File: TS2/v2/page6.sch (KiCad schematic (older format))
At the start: 16 parts, among them SW2 SINGLE STEP/RUN, SW3 STEP, U10 74LS32, U19 74LS20, U20 74LS74, U21 74LS161, U22 74LS161, U23 74LS74, U4 74LS06, U5 74LS04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

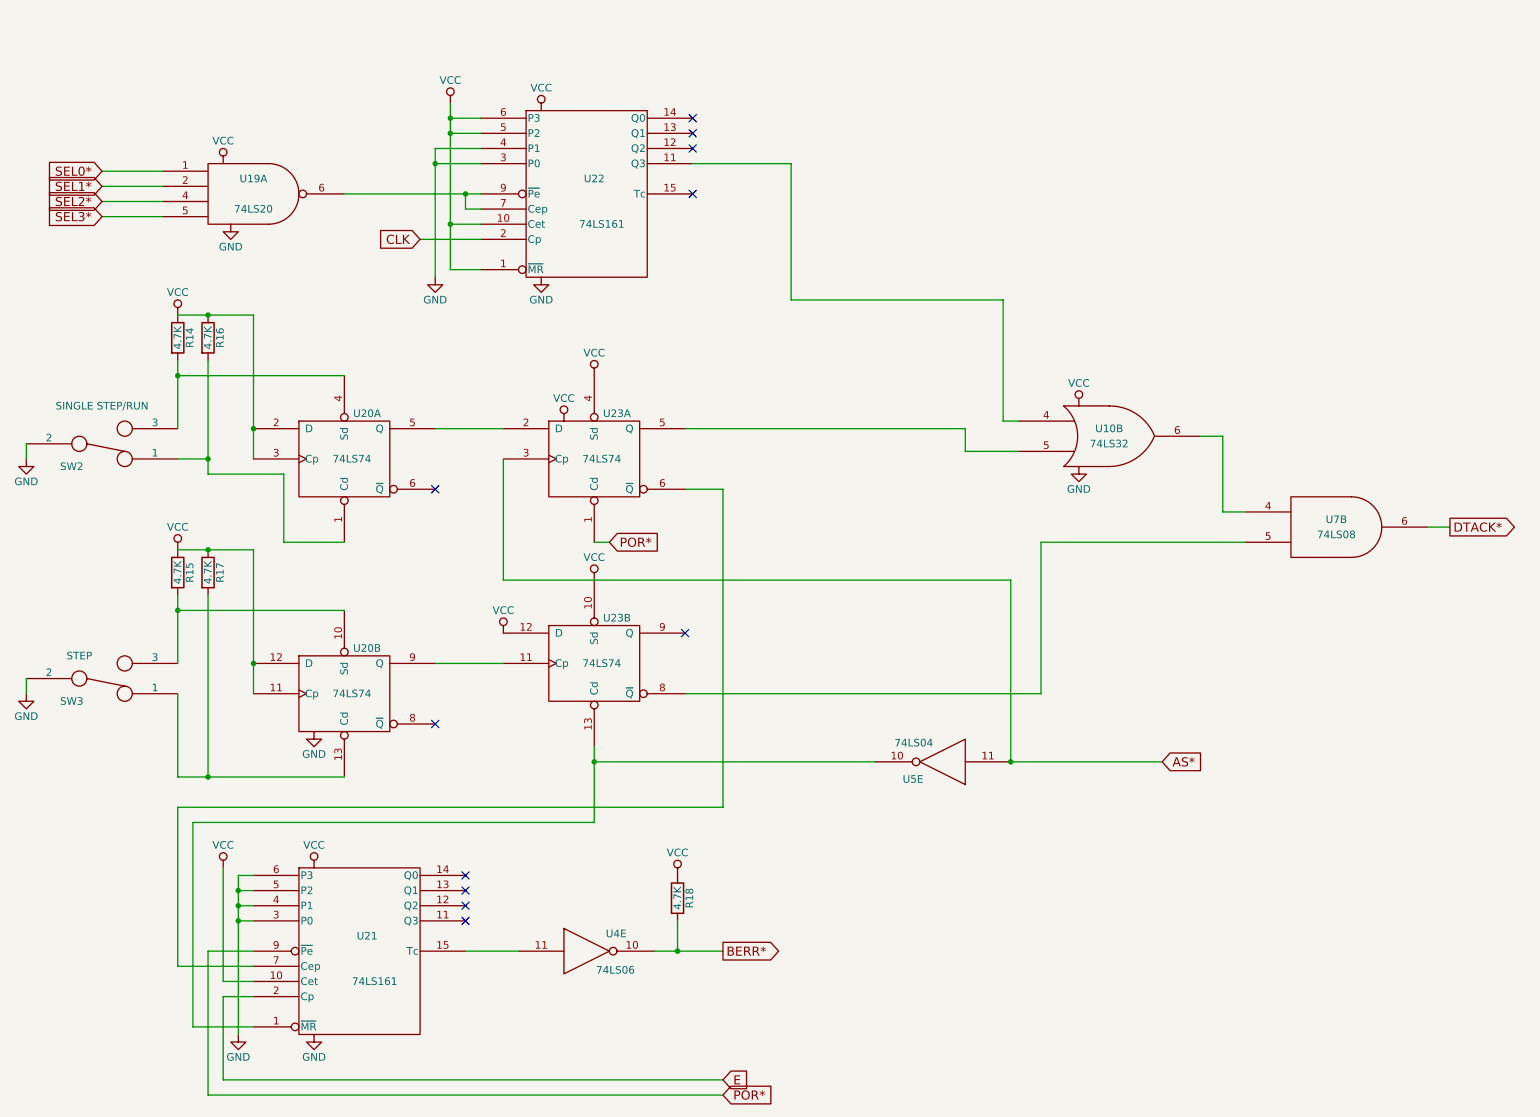
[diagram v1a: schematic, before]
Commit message: Add jumpers for wait states, add some more text.
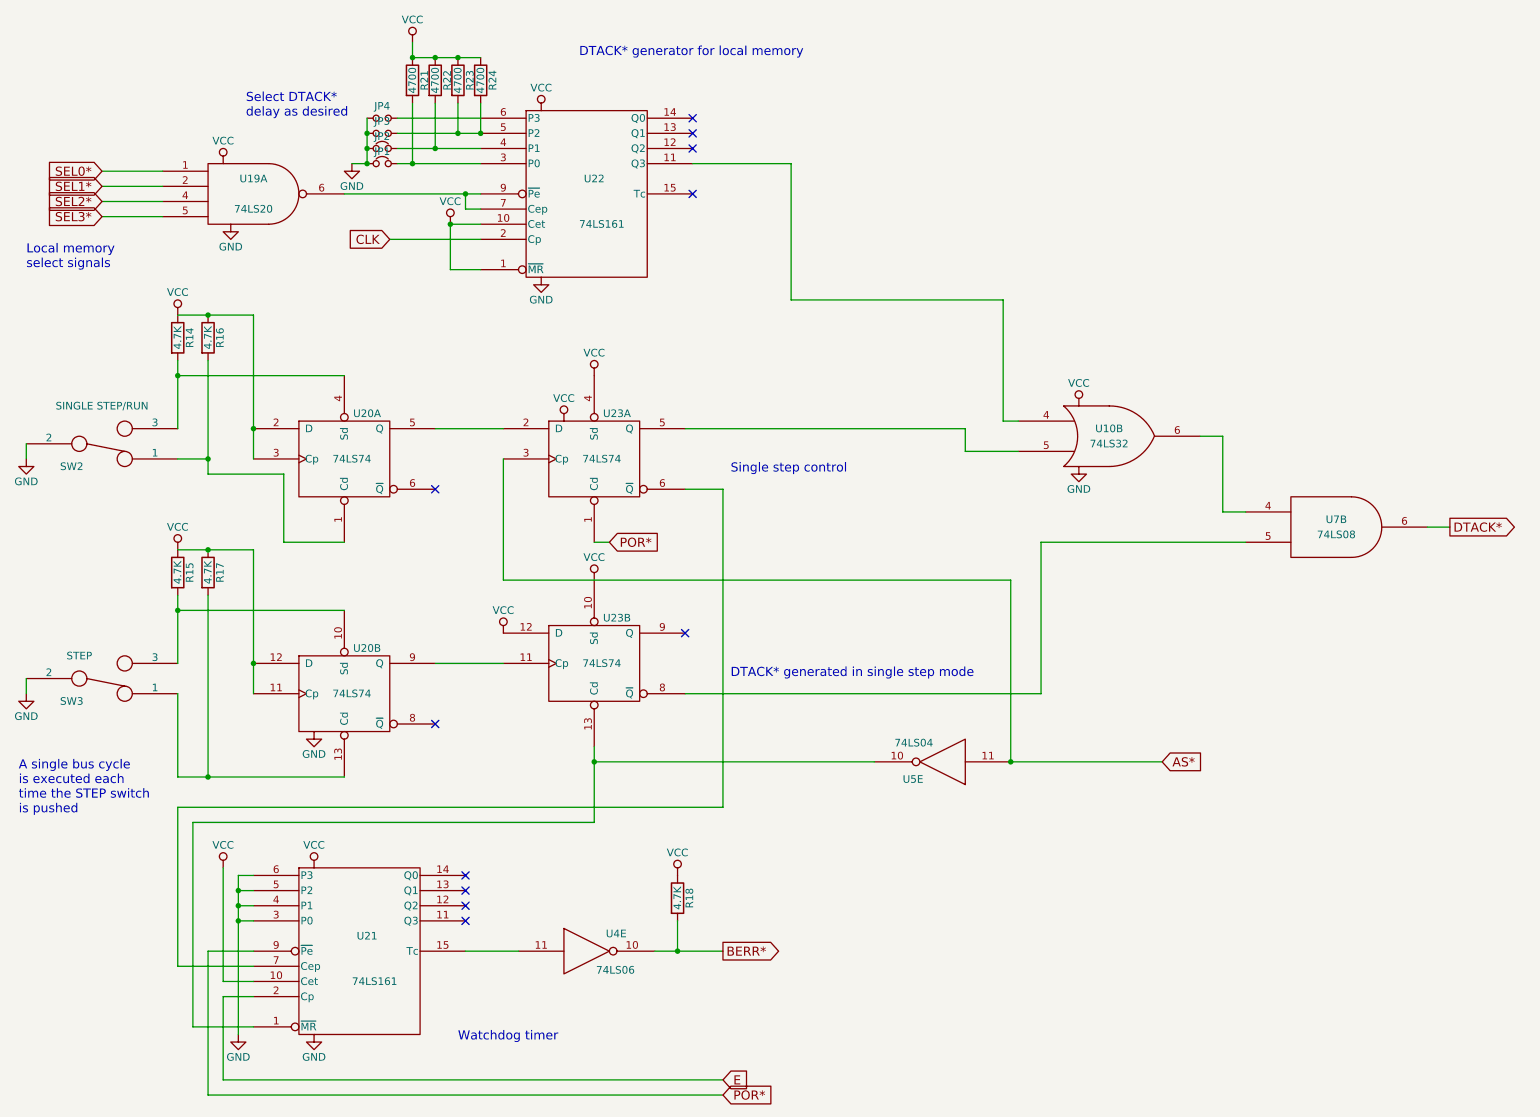
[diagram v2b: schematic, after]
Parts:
- added JP1, JP2: Jumper_NC_Small, symbol Jumper_NC_Small
- added JP3, JP4: Jumper_NO_Small, symbol Jumper_NO_Small
- added R21, R22, R23, R24: 4700, symbol R
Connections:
- net GND: now also JP1.1, JP2.1, JP3.1, JP4.1; no longer U22.3 (P0), U22.4 (P1)
- net VCC: now also R21.1, R22.1, R23.1, R24.1; no longer U22.5 (P2), U22.6 (P3)
- new net: JP1.2, R21.2, U22.3 (P0)
- new net: JP2.2, R22.2, U22.4 (P1)
- new net: JP3.2, R23.2, R24.2, U22.5 (P2)
- new net: JP4.2, U22.6 (P3)
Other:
- note added: "A single bus cycle\nis executed each\ntime the STEP switch\nis pushed"
- note added: "DTACK* generated in single step mode"
- note added: "DTACK* generator for local memory"
- note added: "Local memory\nselect signals"
- note added: "Select DTACK*\ndelay as desired"
- note added: "Single step control"
- note added: "Watchdog timer"
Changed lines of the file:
@@
-$EndComp
-$Comp
-L 74LS161 U22
-U 1 1 57C4D9FF
-P 4400 1800
-F 0 "U22" H 4450 1900 50  0000 C CNN
-F 1 "74LS161" H 4500 1600 50  0000 C CNN
-F 2 "" H 4400 1800 50  0000 C CNN
-F 3 "" H 4400 1800 50  0000 C CNN
-	1    4400 1800
-	1    0    0    -1
 $EndComp
 $Comp
@@
 	-1   0    0    1
 $EndComp
-Text GLabel 3300 2100 0    60   Input ~ 0
+Text GLabel 3100 2100 0    60   Input ~ 0
 CLK
 $Comp
@@
 L VCC #PWR062
 U 1 1 57CB85CC
-P 3500 1200
-F 0 "#PWR062" H 3500 1050 50  0001 C CNN
-F 1 "VCC" H 3500 1350 50  0000 C CNN
-F 2 "" H 3500 1200 50  0000 C CNN
-F 3 "" H 3500 1200 50  0000 C CNN
-	1    3500 1200
+P 3500 2000
+F 0 "#PWR062" H 3500 1850 50  0001 C CNN
+F 1 "VCC" H 3500 2150 50  0000 C CNN
+F 2 "" H 3500 2000 50  0000 C CNN
+F 3 "" H 3500 2000 50  0000 C CNN
+	1    3500 2000
 	1    0    0    -1
 $EndComp
@@
 L GND #PWR063
 U 1 1 57CB85CD
-P 3400 2350
-F 0 "#PWR063" H 3400 2100 50  0001 C CNN
-F 1 "GND" H 3400 2200 50  0000 C CNN
-F 2 "" H 3400 2350 50  0000 C CNN
-F 3 "" H 3400 2350 50  0000 C CNN
-	1    3400 2350
+P 2850 1600
+F 0 "#PWR063" H 2850 1350 50  0001 C CNN
+F 1 "GND" H 2850 1450 50  0000 C CNN
+F 2 "" H 2850 1600 50  0000 C CNN
+F 3 "" H 2850 1600 50  0000 C CNN
+	1    2850 1600
 	1    0    0    -1
 $EndComp
@@
 	3500 2000 3700 2000
 Wire Wire Line
-	3500 1200 3500 2300
-Wire Wire Line
 	3500 2300 3700 2300
-Wire Wire Line
-	3500 1400 3700 1400
 Connection ~ 3500 2000
 Wire Wire Line
-	3500 1300 3700 1300
-Connection ~ 3500 1400
-Connection ~ 3500 1300
-Wire Wire Line
-	3700 1500 3400 1500
-Wire Wire Line
-	3400 1500 3400 2350
-Wire Wire Line
-	3700 1600 3400 1600
-Connection ~ 3400 1600
-Wire Wire Line
-	3300 2100 3700 2100
+	3100 2100 3700 2100
 Wire Wire Line
 	5100 1600 5750 1600
@@
 	1    0    0    -1
 $EndComp
+$Comp
+L Jumper_NC_Small JP1
+U 1 1 57D82D4E
+P 3050 1600
+F 0 "JP1" H 3050 1680 50  0000 C CNN
+F 1 "Jumper_NC_Small" H 3060 1540 50  0001 C CNN
+F 2 "" H 3050 1600 50  0000 C CNN
+F 3 "" H 3050 1600 50  0000 C CNN
+	1    3050 1600
+	1    0    0    -1
+$EndComp
+$Comp
+L Jumper_NO_Small JP3
+U 1 1 57D82D8D
+P 3050 1400
+F 0 "JP3" H 3050 1480 50  0000 C CNN
+F 1 "Jumper_NO_Small" H 3060 1340 50  0001 C CNN
+F 2 "" H 3050 1400 50  0000 C CNN
+F 3 "" H 3050 1400 50  0000 C CNN
+	1    3050 1400
+	1    0    0    -1
+$EndComp
+Wire Wire Line
+	3500 2000 3500 2300
+Wire Wire Line
+	3150 1300 3700 1300
+Wire Wire Line
+	3150 1400 3700 1400
+Wire Wire Line
+	3150 1500 3700 1500
+Wire Wire Line
+	3150 1600 3700 1600
+$Comp
+L R R24
+U 1 1 57D834D0
+P 3700 1050
+F 0 "R24" V 3780 1050 50  0000 C CNN
+F 1 "4700" V 3700 1050 50  0000 C CNN
+F 2 "" V 3630 1050 50  0000 C CNN
+F 3 "" H 3700 1050 50  0000 C CNN
+	1    3700 1050
+	1    0    0    -1
+$EndComp
+$Comp
+L R R23
+U 1 1 57D8361D
+P 3550 1050
+F 0 "R23" V 3630 1050 50  0000 C CNN
+F 1 "4700" V 3550 1050 50  0000 C CNN
+F 2 "" V 3480 1050 50  0000 C CNN
+F 3 "" H 3550 1050 50  0000 C CNN
+	1    3550 1050
+	1    0    0    -1
+$EndComp
+$Comp
+L R R22
+U 1 1 57D8366F
+P 3400 1050
+F 0 "R22" V 3480 1050 50  0000 C CNN
+F 1 "4700" V 3400 1050 50  0000 C CNN
+F 2 "" V 3330 1050 50  0000 C CNN
+F 3 "" H 3400 1050 50  0000 C CNN
+	1    3400 1050
+	1    0    0    -1
+$EndComp
+$Comp
+L R R21
+U 1 1 57D8398D
+P 3250 1050
+F 0 "R21" V 3330 1050 50  0000 C CNN
+F 1 "4700" V 3250 1050 50  0000 C CNN
+F 2 "" V 3180 1050 50  0000 C CNN
+F 3 "" H 3250 1050 50  0000 C CNN
+	1    3250 1050
+	1    0    0    -1
+$EndComp
+$Comp
+L Jumper_NO_Small JP4
+U 1 1 57D842DD
+P 3050 1300
+F 0 "JP4" H 3050 1380 50  0000 C CNN
+F 1 "Jumper_NO_Small" H 3060 1240 50  0001 C CNN
+F 2 "" H 3050 1300 50  0000 C CNN
+F 3 "" H 3050 1300 50  0000 C CNN
+	1    3050 1300
+	1    0    0    -1
+$EndComp
+$Comp
+L Jumper_NC_Small JP2
+U 1 1 57D84338
+P 3050 1500
+F 0 "JP2" H 3050 1580 50  0000 C CNN
+F 1 "Jumper_NC_Small" H 3060 1440 50  0001 C CNN
+F 2 "" H 3050 1500 50  0000 C CNN
+F 3 "" H 3050 1500 50  0000 C CNN
+	1    3050 1500
+	1    0    0    -1
+$EndComp
+Wire Wire Line
+	2950 1600 2850 1600
+Wire Wire Line
+	2950 1300 2950 1600
+Connection ~ 2950 1500
+Connection ~ 2950 1400
+Wire Wire Line
+	3250 1200 3250 1600
+Connection ~ 3250 1600
+Wire Wire Line
+	3400 1200 3400 1500
+Connection ~ 3400 1500
+Wire Wire Line
+	3550 1200 3550 1400
+Connection ~ 3550 1400
+Wire Wire Line
+	3700 1400 3700 1200
+Connection ~ 3700 1400
+Connection ~ 2950 1600
+Wire Wire Line
+	3250 900  3700 900
+Connection ~ 3550 900
+Connection ~ 3400 900
+Wire Wire Line
+	3250 800  3250 900
+$Comp
+L VCC #PWR079
+U 1 1 57D85188
+P 3250 800
+F 0 "#PWR079" H 3250 650 50  0001 C CNN
+F 1 "VCC" H 3250 950 50  0000 C CNN
+F 2 "" H 3250 800 50  0000 C CNN
+F 3 "" H 3250 800 50  0000 C CNN
+	1    3250 800
+	1    0    0    -1
+$EndComp
+Connection ~ 3250 900
+Text Notes 2150 1300 0    60   ~ 0
+Select DTACK*\ndelay as desired
+$Comp
+L 74LS161 U22
+U 1 1 57C4D9FF
+P 4400 1800
+F 0 "U22" H 4450 1900 50  0000 C CNN
+F 1 "74LS161" H 4500 1600 50  0000 C CNN
+F 2 "" H 4400 1800 50  0000 C CNN
+F 3 "" H 4400 1800 50  0000 C CNN
+	1    4400 1800
+	1    0    0    -1
+$EndComp
+Text Notes 3550 7400 0    60   ~ 0
+Watchdog timer
+Text Notes 5350 5000 0    60   ~ 0
+DTACK* generated in single step mode
+Text Notes 650  5900 0    60   ~ 0
+A single bus cycle\nis executed each\ntime the STEP switch\nis pushed
+Text Notes 5350 3650 0    60   ~ 0
+Single step control
+Text Notes 700  2300 0    60   ~ 0
+Local memory\nselect signals
+Text Notes 4350 900  0    60   ~ 0
+DTACK* generator for local memory
 $EndSCHEMATC

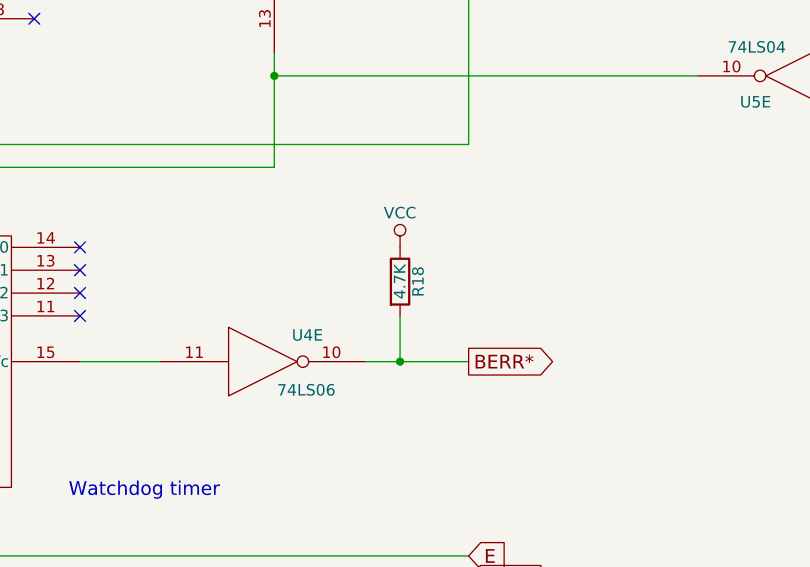
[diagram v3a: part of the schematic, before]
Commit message: Remove two duplicated pullup resistors. Route some signals better.
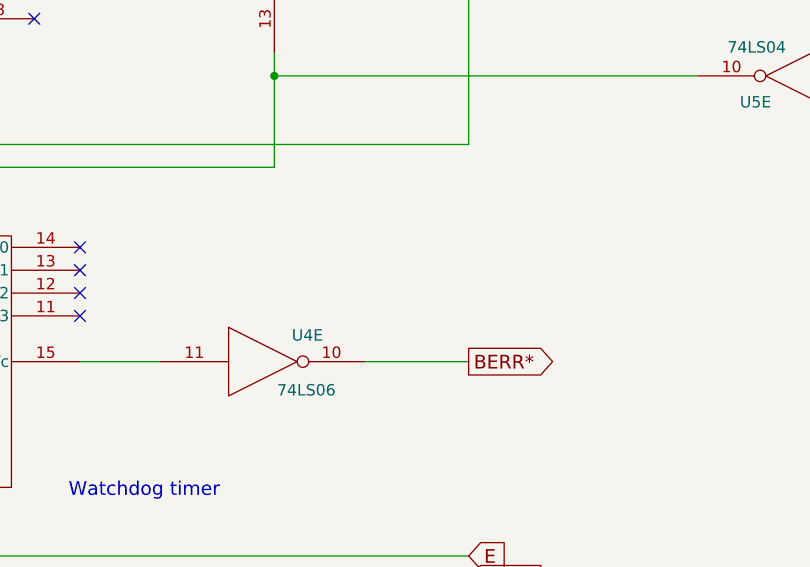
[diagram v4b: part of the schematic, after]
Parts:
- removed R18: 4.7K, symbol R
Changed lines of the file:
@@
 Sheet 7 8
 Title "TS2 68000 Single Board Computer"
-Date "2016-09-03"
+Date "2016-11-27"
 Rev "2.0"
 Comp "Jeff Tranter"
@@
 Text GLabel 5300 6800 2    60   Output ~ 0
 BERR*
-$Comp
-L R R18
-U 1 1 57CB85C4
-P 5000 6450
-F 0 "R18" V 5080 6450 50  0000 C CNN
-F 1 "4.7K" V 5000 6450 50  0000 C CNN
-F 2 "" V 4930 6450 50  0000 C CNN
-F 3 "" H 5000 6450 50  0000 C CNN
-	1    5000 6450
-	1    0    0    -1
-$EndComp
-$Comp
-L VCC #PWR059
-U 1 1 57C53581
-P 5000 6300
-F 0 "#PWR059" H 5000 6150 50  0001 C CNN
-F 1 "VCC" H 5000 6450 50  0000 C CNN
-F 2 "" H 5000 6300 50  0000 C CNN
-F 3 "" H 5000 6300 50  0000 C CNN
-	1    5000 6300
-	1    0    0    -1
-$EndComp
 Text GLabel 1200 1650 0    60   Input ~ 0
 SEL0*
@@
 SEL3*
 $Comp
-L GND #PWR060
+L GND #PWR058
 U 1 1 57C5544E
 P 700 3550
-F 0 "#PWR060" H 700 3300 50  0001 C CNN
+F 0 "#PWR058" H 700 3300 50  0001 C CNN
 F 1 "GND" H 700 3400 50  0000 C CNN
 F 2 "" H 700 3550 50  0000 C CNN
@@
 $EndComp
 $Comp
-L GND #PWR061
+L GND #PWR059
 U 1 1 57C55480
 P 700 5100
-F 0 "#PWR061" H 700 4850 50  0001 C CNN
+F 0 "#PWR059" H 700 4850 50  0001 C CNN
 F 1 "GND" H 700 4950 50  0000 C CNN
 F 2 "" H 700 5100 50  0000 C CNN
@@
 POR*
 $Comp
-L GND #PWR062
+L GND #PWR060
 U 1 1 57CB85CA
 P 4100 2350
-F 0 "#PWR062" H 4100 2100 50  0001 C CNN
+F 0 "#PWR060" H 4100 2100 50  0001 C CNN
 F 1 "GND" H 4100 2200 50  0000 C CNN
 F 2 "" H 4100 2350 50  0000 C CNN
@@
 $EndComp
 $Comp
-L VCC #PWR063
+L VCC #PWR061
 U 1 1 57CB85CB
 P 4100 1250
-F 0 "#PWR063" H 4100 1100 50  0001 C CNN
+F 0 "#PWR061" H 4100 1100 50  0001 C CNN
 F 1 "VCC" H 4100 1400 50  0000 C CNN
 F 2 "" H 4100 1250 50  0000 C CNN
@@
 $EndComp
 $Comp
-L VCC #PWR064
+L VCC #PWR062
 U 1 1 57CB85CC
 P 3500 2000
-F 0 "#PWR064" H 3500 1850 50  0001 C CNN
+F 0 "#PWR062" H 3500 1850 50  0001 C CNN
 F 1 "VCC" H 3500 2150 50  0000 C CNN
 F 2 "" H 3500 2000 50  0000 C CNN
@@
 $EndComp
 $Comp
-L GND #PWR065
+L GND #PWR063
 U 1 1 57CB85CD
 P 2850 1600
-F 0 "#PWR065" H 2850 1350 50  0001 C CNN
+F 0 "#PWR063" H 2850 1350 50  0001 C CNN
 F 1 "GND" H 2850 1450 50  0000 C CNN
 F 2 "" H 2850 1600 50  0000 C CNN
@@
 NoConn ~ 5100 1800
 $Comp
-L GND #PWR066
+L GND #PWR064
 U 1 1 57CB85CE
 P 2600 7350
-F 0 "#PWR066" H 2600 7100 50  0001 C CNN
+F 0 "#PWR064" H 2600 7100 50  0001 C CNN
 F 1 "GND" H 2600 7200 50  0000 C CNN
 F 2 "" H 2600 7350 50  0000 C CNN
@@
 $EndComp
 $Comp
-L VCC #PWR067
+L VCC #PWR065
 U 1 1 57CB85CF
 P 2600 6250
-F 0 "#PWR067" H 2600 6100 50  0001 C CNN
+F 0 "#PWR065" H 2600 6100 50  0001 C CNN
 F 1 "VCC" H 2600 6400 50  0000 C CNN
 F 2 "" H 2600 6250 50  0000 C CNN
@@
 $EndComp
 $Comp
-L GND #PWR068
+L GND #PWR066
 U 1 1 57CB85D0
 P 2100 7350
-F 0 "#PWR068" H 2100 7100 50  0001 C CNN
+F 0 "#PWR066" H 2100 7100 50  0001 C CNN
 F 1 "GND" H 2100 7200 50  0000 C CNN
 F 2 "" H 2100 7350 50  0000 C CNN
@@
 NoConn ~ 3600 6600
 $Comp
-L VCC #PWR069
+L VCC #PWR067
 U 1 1 57CB85D1
 P 2000 6250
-F 0 "#PWR069" H 2000 6100 50  0001 C CNN
+F 0 "#PWR067" H 2000 6100 50  0001 C CNN
 F 1 "VCC" H 2000 6400 50  0000 C CNN
 F 2 "" H 2000 6250 50  0000 C CNN
@@
 	4850 6800 5300 6800
 Wire Wire Line
-	5000 6800 5000 6600
-Connection ~ 5000 6800
-Wire Wire Line
 	3600 6800 3950 6800
 Wire Wire Line
@@
 Connection ~ 1900 2600
 $Comp
-L VCC #PWR070
+L VCC #PWR068
 U 1 1 57CB85D4
 P 1700 2600
-F 0 "#PWR070" H 1700 2450 50  0001 C CNN
+F 0 "#PWR068" H 1700 2450 50  0001 C CNN
 F 1 "VCC" H 1700 2750 50  0000 C CNN
 F 2 "" H 1700 2600 50  0000 C CNN
@@
 Connection ~ 1700 4550
 $Comp
-L VCC #PWR071
+L VCC #PWR069
 U 1 1 57C62B87
 P 1700 4150
-F 0 "#PWR071" H 1700 4000 50  0001 C CNN
+F 0 "#PWR069" H 1700 4000 50  0001 C CNN
 F 1 "VCC" H 1700 4300 50  0000 C CNN
 F 2 "" H 1700 4150 50  0000 C CNN
@@
 Connection ~ 1900 5650
 $Comp
-L VCC #PWR072
+L VCC #PWR070
 U 1 1 57C63574
 P 4450 3000
-F 0 "#PWR072" H 4450 2850 50  0001 C CNN
+F 0 "#PWR070" H 4450 2850 50  0001 C CNN
 F 1 "VCC" H 4450 3150 50  0000 C CNN
 F 2 "" H 4450 3000 50  0000 C CNN
@@
 $EndComp
 $Comp
-L VCC #PWR073
+L VCC #PWR071
 U 1 1 57C635B0
 P 4450 4350
-F 0 "#PWR073" H 4450 4200 50  0001 C CNN
+F 0 "#PWR071" H 4450 4200 50  0001 C CNN
 F 1 "VCC" H 4450 4500 50  0000 C CNN
 F 2 "" H 4450 4350 50  0000 C CNN
@@
 	7400 4100 8750 4100
 $Comp
-L VCC #PWR074
+L VCC #PWR072
 U 1 1 57C63E0E
 P 3850 4700
-F 0 "#PWR074" H 3850 4550 50  0001 C CNN
+F 0 "#PWR072" H 3850 4550 50  0001 C CNN
 F 1 "VCC" H 3850 4850 50  0000 C CNN
 F 2 "" H 3850 4700 50  0000 C CNN
@@
 	5300 3750 5050 3750
 $Comp
-L GND #PWR075
+L GND #PWR073
 U 1 1 57C65008
 P 2050 2000
-F 0 "#PWR075" H 2050 1750 50  0001 C CNN
+F 0 "#PWR073" H 2050 1750 50  0001 C CNN
 F 1 "GND" H 2050 1850 50  0000 C CNN
 F 2 "" H 2050 2000 50  0000 C CNN
@@
 $EndComp
 $Comp
-L VCC #PWR076
+L VCC #PWR074
 U 1 1 57C65080
 P 2000 1600
-F 0 "#PWR076" H 2000 1450 50  0001 C CNN
+F 0 "#PWR074" H 2000 1450 50  0001 C CNN
 F 1 "VCC" H 2000 1750 50  0000 C CNN
 F 2 "" H 2000 1600 50  0000 C CNN
@@
 $EndComp
 $Comp
-L GND #PWR077
+L GND #PWR075
 U 1 1 57CB85DD
 P 2600 5350
-F 0 "#PWR077" H 2600 5100 50  0001 C CNN
+F 0 "#PWR075" H 2600 5100 50  0001 C CNN
 F 1 "GND" H 2600 5200 50  0000 C CNN
 F 2 "" H 2600 5350 50  0000 C CNN
@@
 $EndComp
 $Comp
-L VCC #PWR078
+L VCC #PWR076
 U 1 1 57C9F798
 P 4250 3300
-F 0 "#PWR078" H 4250 3150 50  0001 C CNN
+F 0 "#PWR076" H 4250 3150 50  0001 C CNN
 F 1 "VCC" H 4250 3450 50  0000 C CNN
 F 2 "" H 4250 3300 50  0000 C CNN
@@
 Connection ~ 7200 5550
 $Comp
-L GND #PWR079
+L GND #PWR077
 U 1 1 57CB624C
 P 7650 3600
-F 0 "#PWR079" H 7650 3350 50  0001 C CNN
+F 0 "#PWR077" H 7650 3350 50  0001 C CNN
 F 1 "GND" H 7650 3450 50  0000 C CNN
 F 2 "" H 7650 3600 50  0000 C CNN
@@
 $EndComp
 $Comp
-L VCC #PWR080
+L VCC #PWR078
 U 1 1 57CB85E0
 P 7650 3200
-F 0 "#PWR080" H 7650 3050 50  0001 C CNN
+F 0 "#PWR078" H 7650 3050 50  0001 C CNN
 F 1 "VCC" H 7650 3350 50  0000 C CNN
 F 2 "" H 7650 3200 50  0000 C CNN
@@
 	3250 800  3250 900
 $Comp
-L VCC #PWR081
+L VCC #PWR079
 U 1 1 57D85188
 P 3250 800
-F 0 "#PWR081" H 3250 650 50  0001 C CNN
+F 0 "#PWR079" H 3250 650 50  0001 C CNN
 F 1 "VCC" H 3250 950 50  0000 C CNN
 F 2 "" H 3250 800 50  0000 C CNN

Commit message: Move some labels to make them more readable.
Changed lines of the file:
@@
 U 1 1 57D82D4E
 P 3050 1600
-F 0 "JP1" H 3050 1680 50  0000 C CNN
+F 0 "JP1" H 2750 1600 50  0000 C CNN
 F 1 "Jumper_NC_Small" H 3060 1540 50  0001 C CNN
 F 2 "" H 3050 1600 50  0000 C CNN
@@
 U 1 1 57D82D8D
 P 3050 1400
-F 0 "JP3" H 3050 1480 50  0000 C CNN
+F 0 "JP3" H 2750 1400 50  0000 C CNN
 F 1 "Jumper_NO_Small" H 3060 1340 50  0001 C CNN
 F 2 "" H 3050 1400 50  0000 C CNN
@@
 U 1 1 57D842DD
 P 3050 1300
-F 0 "JP4" H 3050 1380 50  0000 C CNN
+F 0 "JP4" H 2750 1300 50  0000 C CNN
 F 1 "Jumper_NO_Small" H 3060 1240 50  0001 C CNN
 F 2 "" H 3050 1300 50  0000 C CNN
@@
 U 1 1 57D84338
 P 3050 1500
-F 0 "JP2" H 3050 1580 50  0000 C CNN
+F 0 "JP2" H 2750 1500 50  0000 C CNN
 F 1 "Jumper_NC_Small" H 3060 1440 50  0001 C CNN
 F 2 "" H 3050 1500 50  0000 C CNN
@@
 $EndComp
 Connection ~ 3250 900
-Text Notes 2150 1300 0    60   ~ 0
+Text Notes 2300 1150 0    60   ~ 0
 Select DTACK*\ndelay as desired
 $Comp
